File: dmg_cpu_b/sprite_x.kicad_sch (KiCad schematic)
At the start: 85 parts

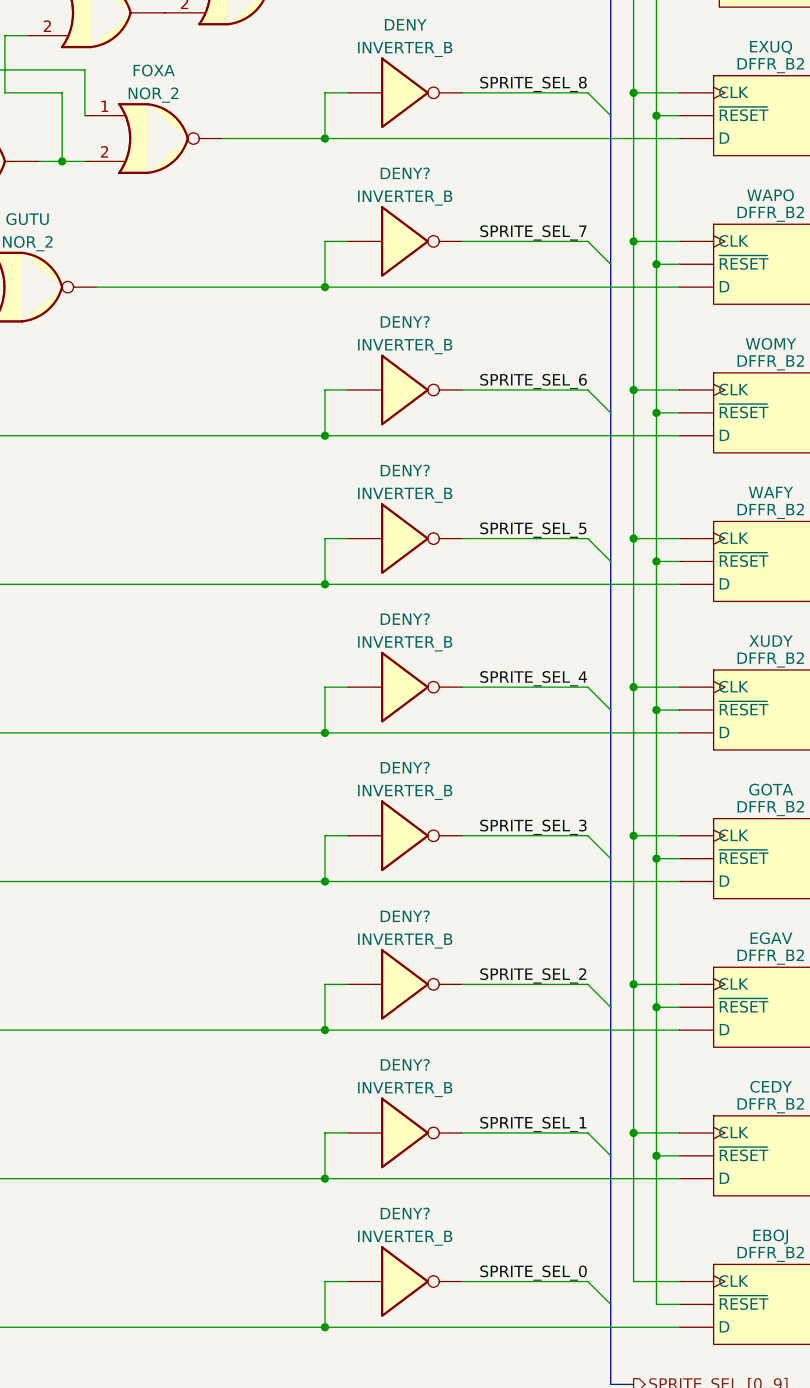
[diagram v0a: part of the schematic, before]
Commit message: sprite y comparator added
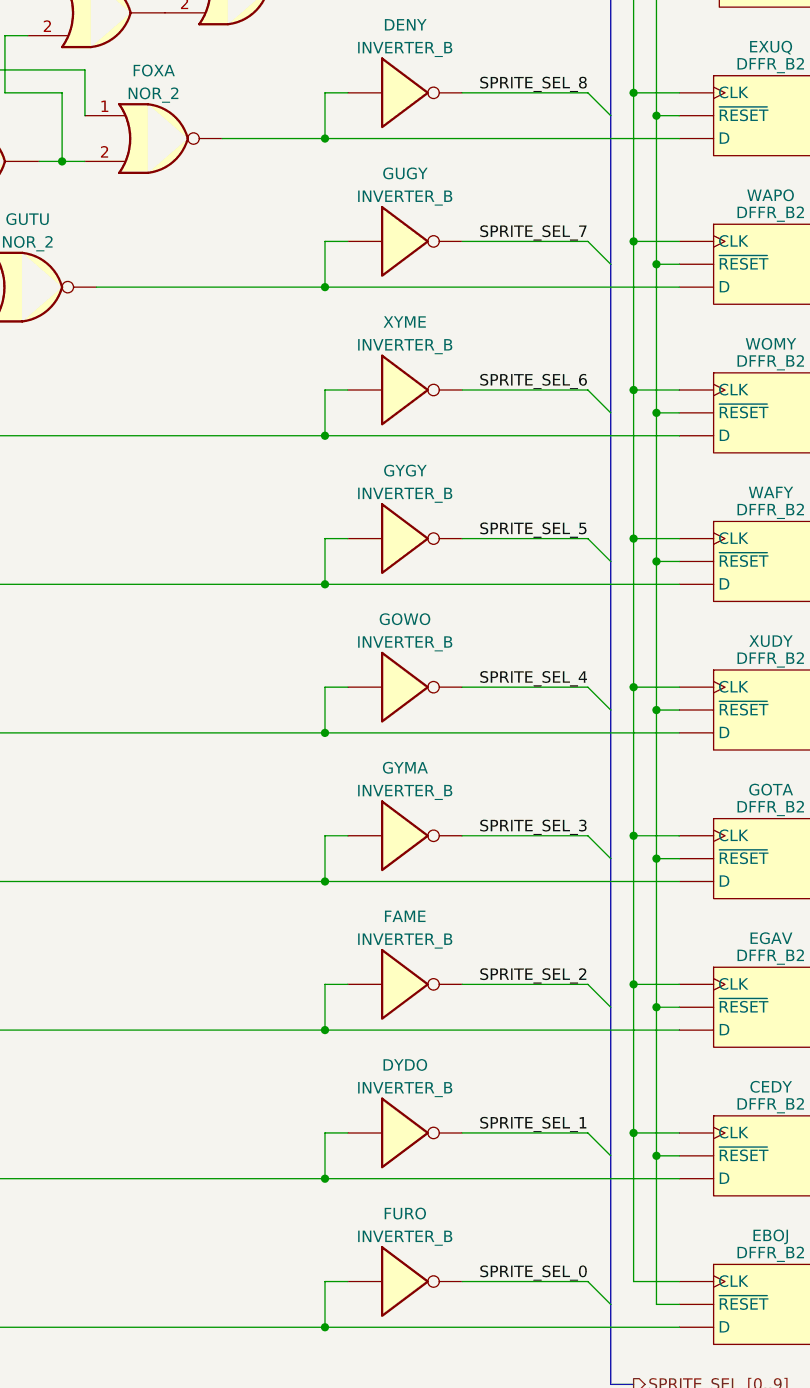
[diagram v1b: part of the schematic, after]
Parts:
- gave numbers to parts that had none: 8
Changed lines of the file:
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@@
   (symbol (lib_id "DMG_CPU_Cells:INVERTER_B") (at 284.48 205.105 0) (unit 1)
     (in_bom yes) (on_board yes) (fields_autoplaced)
-    (property "Reference" "DENY?" (id 0) (at 284.48 197.5952 0))
+    (property "Reference" "FURO" (id 0) (at 284.48 197.5952 0))
     (property "Value" "INVERTER_B" (id 1) (at 284.48 200.1321 0))
     (property "Footprint" "" (id 2) (at 281.94 205.105 0)
@@
   (symbol (lib_id "DMG_CPU_Cells:INVERTER_B") (at 284.48 89.535 0) (unit 1)
     (in_bom yes) (on_board yes) (fields_autoplaced)
-    (property "Reference" "DENY?" (id 0) (at 284.48 82.0252 0))
+    (property "Reference" "GUGY" (id 0) (at 284.48 82.0252 0))
     (property "Value" "INVERTER_B" (id 1) (at 284.48 84.5621 0))
     (property "Footprint" "" (id 2) (at 281.94 89.535 0)
@@
   (symbol (lib_id "DMG_CPU_Cells:INVERTER_B") (at 284.48 172.085 0) (unit 1)
     (in_bom yes) (on_board yes) (fields_autoplaced)
-    (property "Reference" "DENY?" (id 0) (at 284.48 164.5752 0))
+    (property "Reference" "FAME" (id 0) (at 284.48 164.5752 0))
     (property "Value" "INVERTER_B" (id 1) (at 284.48 167.1121 0))
     (property "Footprint" "" (id 2) (at 281.94 172.085 0)
@@
   (symbol (lib_id "DMG_CPU_Cells:INVERTER_B") (at 284.48 188.595 0) (unit 1)
     (in_bom yes) (on_board yes) (fields_autoplaced)
-    (property "Reference" "DENY?" (id 0) (at 284.48 181.0852 0))
+    (property "Reference" "DYDO" (id 0) (at 284.48 181.0852 0))
     (property "Value" "INVERTER_B" (id 1) (at 284.48 183.6221 0))
     (property "Footprint" "" (id 2) (at 281.94 188.595 0)
@@
   (symbol (lib_id "DMG_CPU_Cells:INVERTER_B") (at 284.48 106.045 0) (unit 1)
     (in_bom yes) (on_board yes) (fields_autoplaced)
-    (property "Reference" "DENY?" (id 0) (at 284.48 98.5352 0))
+    (property "Reference" "XYME" (id 0) (at 284.48 98.5352 0))
     (property "Value" "INVERTER_B" (id 1) (at 284.48 101.0721 0))
     (property "Footprint" "" (id 2) (at 281.94 106.045 0)
@@
   (symbol (lib_id "DMG_CPU_Cells:INVERTER_B") (at 284.48 155.575 0) (unit 1)
     (in_bom yes) (on_board yes) (fields_autoplaced)
-    (property "Reference" "DENY?" (id 0) (at 284.48 148.0652 0))
+    (property "Reference" "GYMA" (id 0) (at 284.48 148.0652 0))
     (property "Value" "INVERTER_B" (id 1) (at 284.48 150.6021 0))
     (property "Footprint" "" (id 2) (at 281.94 155.575 0)
@@
   (symbol (lib_id "DMG_CPU_Cells:INVERTER_B") (at 284.48 122.555 0) (unit 1)
     (in_bom yes) (on_board yes) (fields_autoplaced)
-    (property "Reference" "DENY?" (id 0) (at 284.48 115.0452 0))
+    (property "Reference" "GYGY" (id 0) (at 284.48 115.0452 0))
     (property "Value" "INVERTER_B" (id 1) (at 284.48 117.5821 0))
     (property "Footprint" "" (id 2) (at 281.94 122.555 0)
@@
   (symbol (lib_id "DMG_CPU_Cells:INVERTER_B") (at 284.48 139.065 0) (unit 1)
     (in_bom yes) (on_board yes) (fields_autoplaced)
-    (property "Reference" "DENY?" (id 0) (at 284.48 131.5552 0))
+    (property "Reference" "GOWO" (id 0) (at 284.48 131.5552 0))
     (property "Value" "INVERTER_B" (id 1) (at 284.48 134.0921 0))
     (property "Footprint" "" (id 2) (at 281.94 139.065 0)

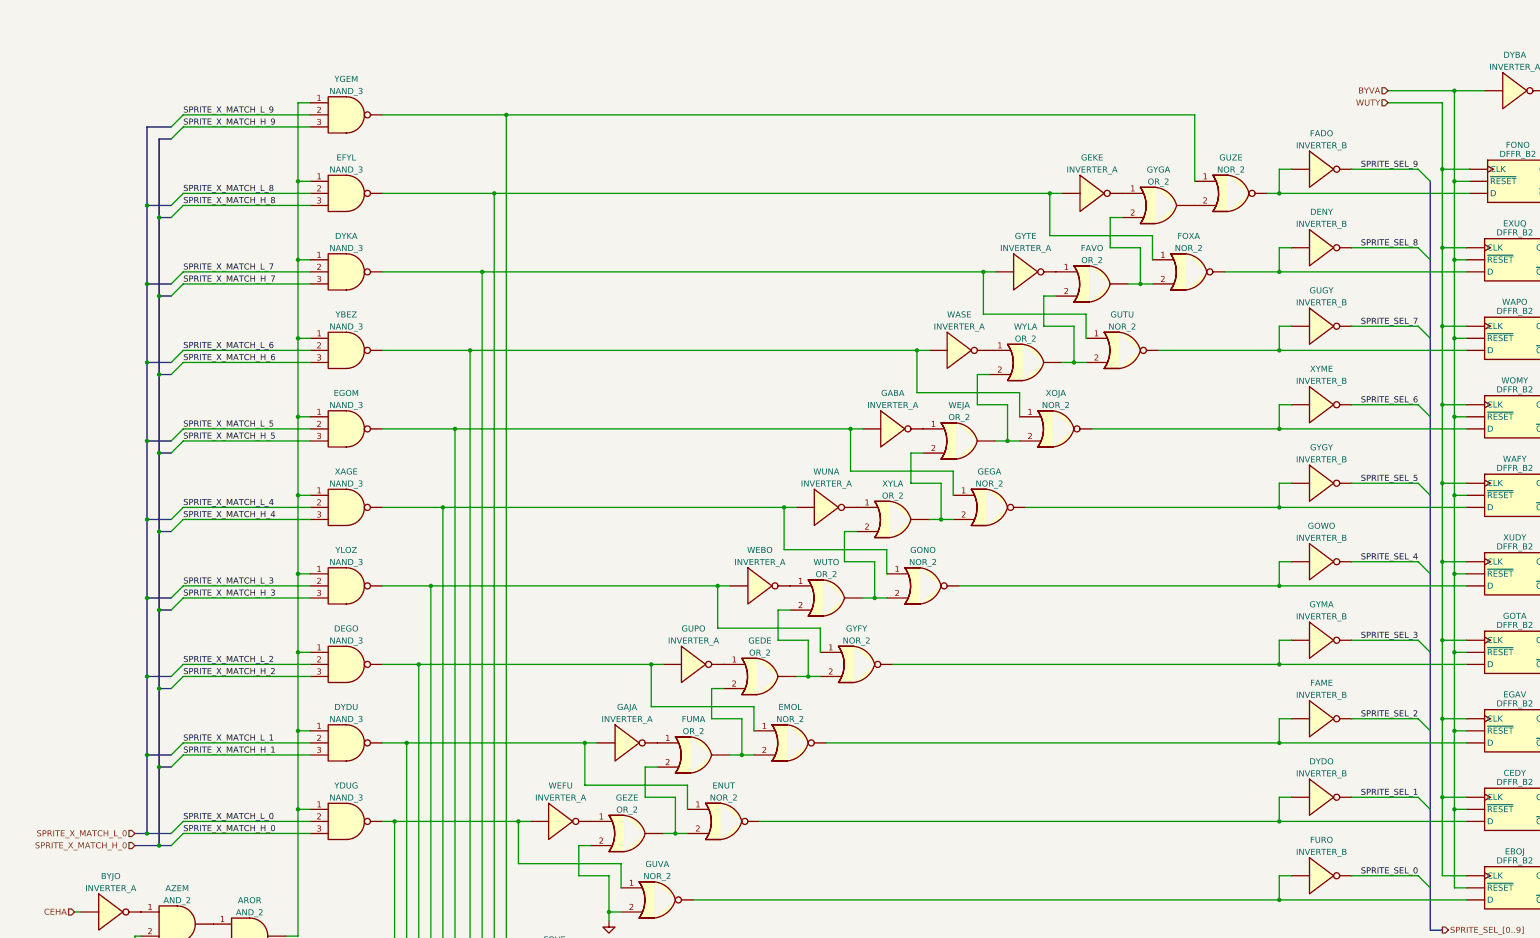
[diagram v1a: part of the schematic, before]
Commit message: more oam sheets added. Some are still work in progress.
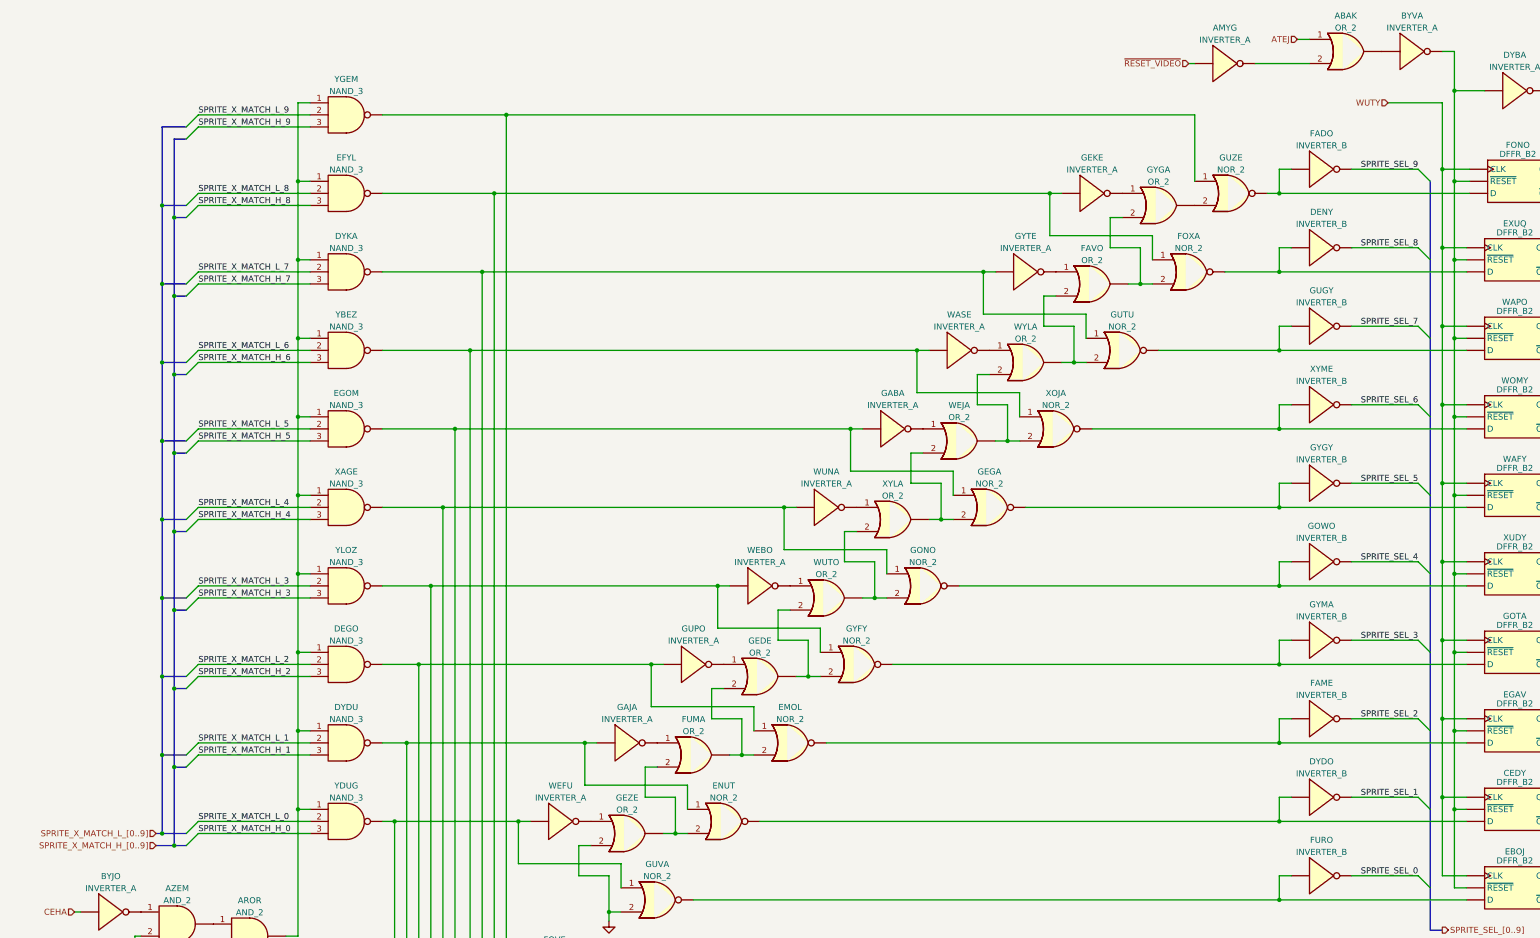
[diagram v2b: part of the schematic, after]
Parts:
- added ABAK: OR_2, symbol DMG_CPU_Cells:OR_2
- added AMYG, BYVA: INVERTER_A, symbol DMG_CPU_Cells:INVERTER_A
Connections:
- net BYVA: no longer names the net of CEDY.2 (~{RESET}), CEDY.4 (~{RESET}), DYBA.1, EBOJ.2 (~{RESET}), EBOJ.4 (~{RESET}), EGAV.2 (~{RESET}), EGAV.4 (~{RESET}), EXUQ.2 (~{RESET}), EXUQ.4 (~{RESET}), FONO.2 (~{RESET}), FONO.4 (~{RESET}), GOTA.2 (~{RESET}), GOTA.4 (~{RESET}), WAFY.2 (~{RESET}), WAFY.4 (~{RESET}), WAPO.2 (~{RESET}), WAPO.4 (~{RESET}), WOMY.2 (~{RESET}), WOMY.4 (~{RESET}), XUDY.2 (~{RESET}), XUDY.4 (~{RESET})
- net BYVA: now also BYVA.2
- new net: ABAK.3, BYVA.1
- new net: ABAK.2, AMYG.2
- new net ATEJ: ABAK.1
- new net ~{RESET_VIDEO}: AMYG.1
